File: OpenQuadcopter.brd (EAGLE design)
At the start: 100 x 100 mm, 36 parts, among them U1 MPU-6000QFN-24

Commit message: update openmotestm
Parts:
- added C10, C13, C14, C15, C16, C17, C18, C19, C20, C21, C22, C23, C8: (no value), openmotestm:C0402
- added C24: (no value), openmotestm:C0603
- added D6, D7: GREEN, openmotestm:LED-0603
- added JP2: USB_MICROB, openmotestm:USB-B-MICRO-SMD_V03
- added R10, R11, R12, R13, R14, R15, R16, R17, R18, R19, R20, R21, R22, R23, R24, R25, R26, R27, R28, R8, R9: (no value), openmotestm:R0402
- added U$13: BQ24075, openmotestm:QFN16
- added U$14: CP2102, openmotestm:QFN28-5X5
- added U$15, U$16: TPS79301, openmotestm:SOT23-6
- added U$17, U$20: 2N7002, openmotestm:SOT23-3
- added U$18: MAX16054, openmotestm:SOT23-6
- added U$19: BUTTON, openmotestm:BUTTON
- added U$21, U$22: 1X2, openmotestm:1X2
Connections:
- new net /CHG: U$13.9
- new net /PGOOD: R17.2, R18.1, U$13.7
- new net AGND: C16.2, C17.2, R14.1, R27.2
- new net DGND: C19.2, C21.1, C23.2, C24.2, D6.C, D7.C, JP2.GND1, R16.1, R28.2, U$14.P$29, U$22.2
- new net EN1: U$13.6
- new net EN2: U$13.5
- new net N$15: R21.1, U$18.4
- new net N$18: R8.2, U$13.12
- new net N$19: R9.2, U$13.14
- new net N$20: R10.2, U$13.16
- new net N$21: R11.2, U$13.1
- new net N$23: R21.2, U$13.15, U$17.3
- new net N$24: C14.1, R12.2, U$15.1, U$15.3
- new net N$25: U$18.1, U$19.P$2
- new net N$26: C15.2, R13.1, R14.2, U$15.5
- new net N$27: C17.1, U$15.4
- new net N$28: C19.1, U$16.4
- new net N$29: C20.2, R15.1, R16.2, R17.1, U$16.5
- new net N$30: C22.1, R24.2, U$20.2
- new net N$32: D6.A, R19.1
- new net N$33: D7.A, R20.1
- new net N$34: R26.1, U$20.3
- new net N$35: JP2.D+1, U$14.P$4
- new net N$36: JP2.D-1, U$14.P$5
- new net SYSOFF: R23.2, U$18.3
- new net V+: C10.1, C13.1, C18.1, C8.1, R12.1, U$13.10, U$13.11, U$13.2, U$13.3, U$16.1, U$16.3
- new net VBUS: C23.1, C24.1, JP2.VBUS1, R22.2, U$13.13, U$14.P$7, U$14.P$8, U$17.1, U$22.1
- new net VCCA: R6.2, R7.2, U$1.13, U$1.2, U$1.4, U1.13, U1.8, U1.9
- new net VCCD: U$11.1
- new net VCOM: R25.2, U$20.1
- net BAT: now also R26.2, U$18.6, U$21.1
- net GND: now also C10.2, C13.2, C14.2, C18.2, C22.2, C8.2, R10.1, R11.1, R22.1, R23.1, R24.1, R25.1, R27.1, R28.1, R8.1, R9.1, U$13.4, U$13.8, U$13.TH, U$15.2, U$16.2, U$17.2, U$18.2, U$21.2
- net PA10: now also U$14.P$26
- net PA11: now also U$14.P$23
- net PA12: now also U$14.P$24
- net PA9: now also U$14.P$25
- net VCC: now also C15.1, C16.1, C20.1, C21.2, R13.2, R15.2, R18.2, R19.2, R20.2, U$15.6, U$16.6; no longer R6.2, R7.2, U$1.13, U$1.2, U$1.4, U$11.1, U1.13, U1.8, U1.9
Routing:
- net VCC: track 71.6 -> 35.7 mm, vias 5 -> 3
- net VCCA: track 0.00 -> 27.3 mm, vias 0 -> 2

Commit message: drawing quadcopter
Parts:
- removed C1, C2: (no value), rcl:C0603
- removed D5: GREEN, openmotestm:LED-0603
- removed R5: (no value), rcl:R0402
- removed U$10: LP5951, openmotestm:SC70
- removed U$21: 1X2, openmotestm:1X2
- moved C23 233.8 mm to (-71.1, 14.0)
- moved C24 233.8 mm to (-71.1, 7.62)
- moved U$22 233.8 mm to (-71.1, 11.4)
- moved R27 233.7 mm to (-83.8, 24.1)
- moved R28 233.7 mm to (-83.8, 20.3)
- moved R26 227.7 mm to (-20.3, 17.8), flipped to the bottom, turned to 180 degrees
- moved C22 224.6 mm to (-24.6, 11.9), flipped to the bottom
- moved R23 222.3 mm to (-71.1, 31.8)
- moved U$19 219.7 mm to (-76.2, 35.6)
- moved R25 218.7 mm to (-21.8, 12.7), flipped to the bottom, turned to 90 degrees
- moved R24 215.3 mm to (-24.6, 13.7), flipped to the bottom, turned to 180 degrees
- moved U$20 213.5 mm to (-22.9, 16.5), flipped to the bottom
- moved U$18 213.4 mm to (-71.1, 36.8)
- moved R22 211.9 mm to (-25.4, 34.3), flipped to the bottom, turned to 180 degrees
- moved U$17 203.6 mm to (-24.1, 30.5), flipped to the bottom, turned to 180 degrees
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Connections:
- removed net N$10: C1.1, U$10.1, U$10.3, U$12.O
- removed net N$17: D5.A, R5.1
- removed net V+: C10.1, C13.1, C18.1, C8.1, R12.1, U$13.10, U$13.11, U$13.2, U$13.3, U$16.1, U$16.3
- removed net VCC: C15.1, C16.1, C2.2, C20.1, C21.2, C5.1, C6.1, C7.1, C9.1, R13.2, R15.2, R18.2, R19.2, R20.2, R5.2, U$10.5, U$15.6, U$16.6
- new net BATTERY_IN: JP1.P1, U$12.P, U$12.S
- net BAT: now also C8.1, U$12.O, U$13.2, U$13.3; no longer JP1.P1, U$12.P, U$12.S, U$21.1
- net GND: no longer C1.2, C2.1, D5.C, U$10.2, U$21.2
- net VCCA: now also C15.1, C16.1, C5.1, C6.1, C7.1, C9.1, R13.2, U$15.6
- net VCCD: now also C20.1, C21.2, R15.2, R18.2, R19.2, R20.2, U$16.6
- net VCOM: now also C10.1, C13.1, C18.1, R12.1, U$13.10, U$13.11, U$16.1, U$16.3
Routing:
- net VCC: track 35.7 -> 0.00 mm, vias 3 -> 0
- net N$10: track 21.8 -> 0.00 mm
- net GND: track 101.9 -> 87.9 mm, vias 8 -> 7
- net VCCA: track 27.3 -> 40.6 mm, vias 2 -> 3
- net BAT: track 148.6 -> 138.4 mm, vias 4 -> 5
- net BATTERY_IN: track 0.00 -> 6.42 mm
- net N$17: track 1.84 -> 0.00 mm

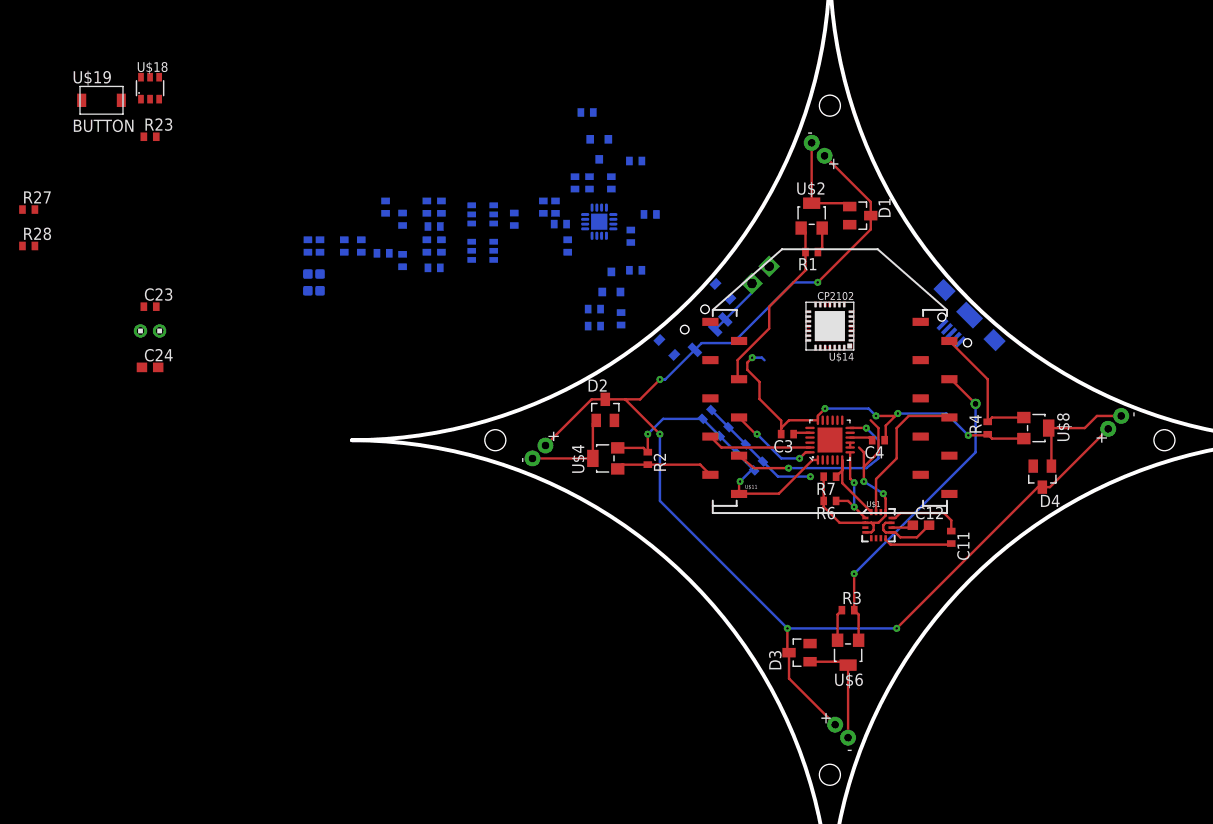
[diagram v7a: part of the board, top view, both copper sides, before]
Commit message: Add XBee-Explorer-Dongle-Sparkfun. Update openmotestm. arrange the layout of openquadcopter board.
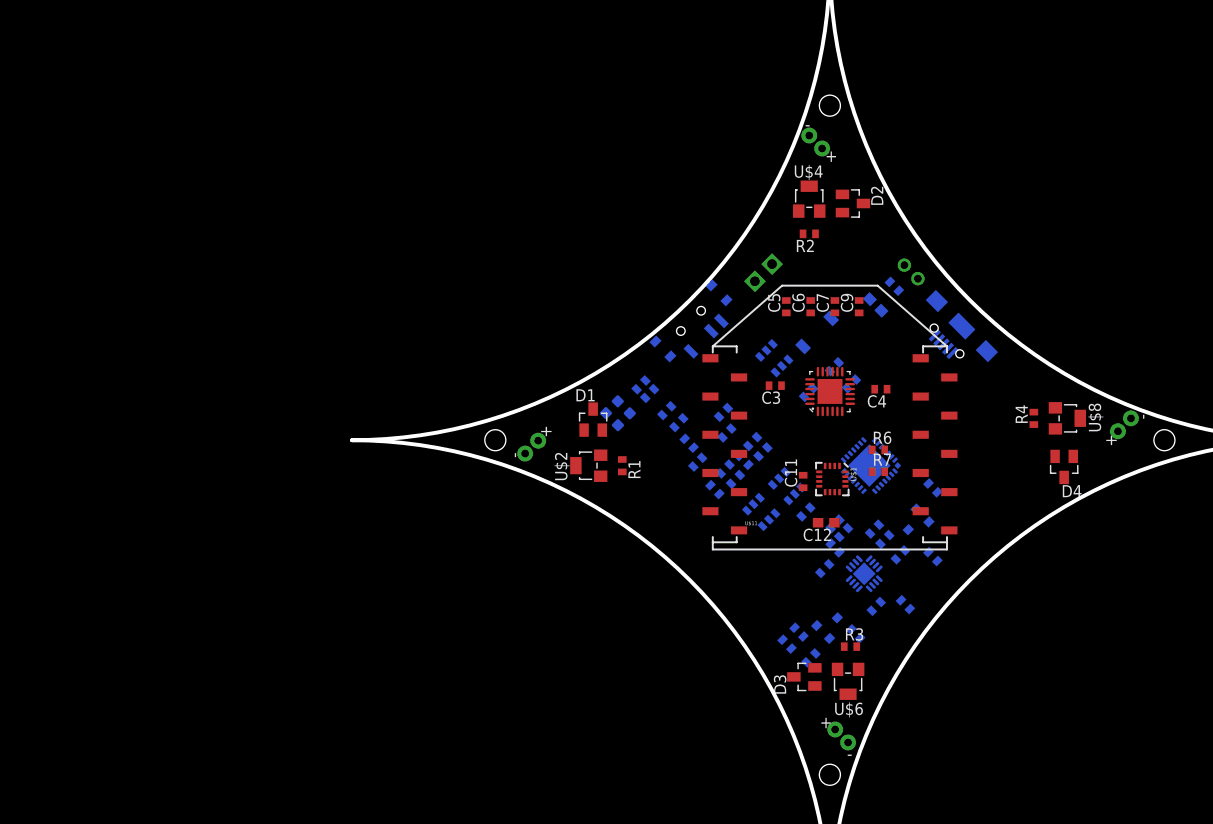
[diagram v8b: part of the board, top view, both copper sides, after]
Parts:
- moved R28 87.3 mm to (2.26, 5.89), flipped to the bottom, turned to 315 degrees
- moved R27 85.9 mm to (0.46, 7.68), flipped to the bottom, turned to 315 degrees
- moved U$22 79.9 mm to (8.50, 17.6), flipped to the bottom, turned to 45 degrees
- moved U$19 78.7 mm to (-1.33, 11.3), flipped to the bottom, turned to 315 degrees
- moved C23 77.9 mm to (6.74, 16.1), flipped to the bottom, turned to 45 degrees
- moved C24 76.2 mm to (4.79, 14.2), flipped to the bottom, turned to 45 degrees
- moved R23 73.9 mm to (-2.23, 4.99), flipped to the bottom, turned to 315 degrees
- moved U$18 71.1 mm to (-5.82, 8.58), flipped to the bottom, turned to 315 degrees
- moved R22 53.4 mm to (10.8, -4.99), turned to 225 degrees
- moved R21 51.8 mm to (10.8, -12.2), turned to 45 degrees
- moved U$17 51.2 mm to (8.98, -8.58), turned to 225 degrees
- moved R10 49.3 mm to (7.36, -12.0), turned to 315 degrees
- moved R11 48.8 mm to (7.90, -17.2), turned to 45 degrees
- moved R9 48.4 mm to (5.75, -10.4), turned to 135 degrees
- moved U$3 48.3 mm to (-34.4, 4.95), turned to 90 degrees
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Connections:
- net PA10 renamed UART_RX
- net PA12 renamed BOOT0
- net PA9 renamed UART_TX
- net RESET: now also U$14.P$28
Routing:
- net BAT: track 138.4 -> 0.00 mm, vias 5 -> 0
- net GND: track 87.9 -> 0.00 mm, vias 7 -> 0
- net VCCA: track 40.6 -> 0.00 mm, vias 3 -> 0
- net MOTOR/PA6: track 34.0 -> 0.00 mm, vias 2 -> 0
- net INT/PA4: track 20.8 -> 0.00 mm, vias 2 -> 0
- net MOTOR/PC8: track 19.0 -> 0.00 mm
- net INT/PC0: track 15.8 -> 0.00 mm
- net MOTOR/PA7: track 14.1 -> 0.00 mm
- net N$7: track 12.2 -> 0.00 mm
- net N$5: track 11.7 -> 0.00 mm
- net SDL/PB6: track 10.9 -> 0.00 mm
- net N$2: track 10.4 -> 0.00 mm
- net N$1: track 10.4 -> 0.00 mm
- net MOTOR/PC9: track 10.3 -> 0.00 mm
- net N$4: track 9.69 -> 0.00 mm, vias 2 -> 0
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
